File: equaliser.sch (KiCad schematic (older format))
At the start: 32 parts, among them U12 NE5532

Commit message: Board is placed and about half-routed
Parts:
- added J9: Conn_01x04_Male, Pin_Headers:Pin_Header_Straight_1x04_Pitch2.54mm, symbol Connector:Conn_01x04_Male
- C66, C67: footprint power:C_Rect_L7.0mm_W4.5mm_P5_1210x2_combo -> power:C_Rect_L19.0mm_W11.0mm_combo
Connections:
- net labels added: VFB, VO
- wire segments 83 -> 87
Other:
- note added: "Port for pluggable RC network\n(Linkwitz Transform Only)"
- moved on the sheet: U12A, U12B
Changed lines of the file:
@@
 L Amplifier_Operational:NE5532 U12
 U 2 1 61877AFD
-P 5100 3800
-F 0 "U12" H 5100 3433 50  0000 C CNN
-F 1 "NE5532" H 5100 3524 50  0000 C CNN
-F 2 "" H 5100 3800 50  0001 C CNN
-F 3 "http://www.ti.com/lit/ds/symlink/ne5532.pdf" H 5100 3800 50  0001 C CNN
-	2    5100 3800
+P 7400 3200
+F 0 "U12" H 7400 2833 50  0000 C CNN
+F 1 "NE5532" H 7400 2924 50  0000 C CNN
+F 2 "" H 7400 3200 50  0001 C CNN
+F 3 "http://www.ti.com/lit/ds/symlink/ne5532.pdf" H 7400 3200 50  0001 C CNN
+	2    7400 3200
 	1    0    0    1
 $EndComp
@@
 U 1 1 61887A13
 P 3600 3200
-F 0 "R68" V 3393 3200 50  0000 C CNN
-F 1 "R2" V 3484 3200 50  0000 C CNN
+F 0 "R68" V 3650 2950 50  0000 C CNN
+F 1 "R2" V 3300 3200 50  0000 C CNN
 F 2 "Resistors_SMD:R_0805" V 3530 3200 50  0001 C CNN
 F 3 "~" H 3600 3200 50  0001 C CNN
@@
 U 1 1 618881D6
 P 3600 3100
-F 0 "R66" V 3393 3100 50  0000 C CNN
-F 1 "R2" V 3484 3100 50  0000 C CNN
+F 0 "R66" V 3600 2850 50  0000 C CNN
+F 1 "R2" V 3300 3100 50  0000 C CNN
 F 2 "Resistors_SMD:R_0805" V 3530 3100 50  0001 C CNN
 F 3 "~" H 3600 3100 50  0001 C CNN
@@
 U 1 1 6188AB3F
 P 3600 3000
-F 0 "R64" V 3393 3000 50  0000 C CNN
-F 1 "R2" V 3484 3000 50  0000 C CNN
+F 0 "R64" V 3600 2750 50  0000 C CNN
+F 1 "R2" V 3300 3000 50  0000 C CNN
 F 2 "Resistors_SMD:R_0805" V 3530 3000 50  0001 C CNN
 F 3 "~" H 3600 3000 50  0001 C CNN
@@
 U 1 1 6188EADB
 P 4800 3200
-F 0 "R69" V 4593 3200 50  0000 C CNN
+F 0 "R69" V 4850 2950 50  0000 C CNN
 F 1 "R2" V 4684 3200 50  0000 C CNN
 F 2 "Resistors_SMD:R_0805" V 4730 3200 50  0001 C CNN
@@
 U 1 1 6188EAE1
 P 4800 3100
-F 0 "R67" V 4593 3100 50  0000 C CNN
+F 0 "R67" V 4800 2850 50  0000 C CNN
 F 1 "R2" V 4684 3100 50  0000 C CNN
 F 2 "Resistors_SMD:R_0805" V 4730 3100 50  0001 C CNN
@@
 U 1 1 6188EAE7
 P 4800 3000
-F 0 "R65" V 4593 3000 50  0000 C CNN
+F 0 "R65" V 4800 2750 50  0000 C CNN
 F 1 "R2" V 4684 3000 50  0000 C CNN
 F 2 "Resistors_SMD:R_0805" V 4730 3000 50  0001 C CNN
@@
 U 1 1 61891898
 P 3600 3900
-F 0 "R75" V 3393 3900 50  0000 C CNN
+F 0 "R75" V 3650 3650 50  0000 C CNN
 F 1 "R1" V 3484 3900 50  0000 C CNN
 F 2 "Resistors_SMD:R_0805" V 3530 3900 50  0001 C CNN
@@
 U 1 1 6189189E
 P 3600 3800
-F 0 "R73" V 3393 3800 50  0000 C CNN
+F 0 "R73" V 3600 3550 50  0000 C CNN
 F 1 "R1" V 3484 3800 50  0000 C CNN
 F 2 "Resistors_SMD:R_0805" V 3530 3800 50  0001 C CNN
@@
 U 1 1 618918A4
 P 3600 3700
-F 0 "R71" V 3393 3700 50  0000 C CNN
+F 0 "R71" V 3600 3450 50  0000 C CNN
 F 1 "R1" V 3484 3700 50  0000 C CNN
 F 2 "Resistors_SMD:R_0805" V 3530 3700 50  0001 C CNN
@@
 U 1 1 61893819
 P 4150 3900
-F 0 "R76" V 3943 3900 50  0000 C CNN
+F 0 "R76" V 4150 4150 50  0000 C CNN
 F 1 "R1" V 4034 3900 50  0000 C CNN
 F 2 "Resistors_SMD:R_0805" V 4080 3900 50  0001 C CNN
@@
 U 1 1 6189381F
 P 4150 3800
-F 0 "R74" V 3943 3800 50  0000 C CNN
+F 0 "R74" V 4150 4050 50  0000 C CNN
 F 1 "R1" V 4034 3800 50  0000 C CNN
 F 2 "Resistors_SMD:R_0805" V 4080 3800 50  0001 C CNN
@@
 U 1 1 61893825
 P 4150 3700
-F 0 "R72" V 3943 3700 50  0000 C CNN
+F 0 "R72" V 4100 3900 50  0000 C CNN
 F 1 "R1" V 4034 3700 50  0000 C CNN
 F 2 "Resistors_SMD:R_0805" V 4080 3700 50  0001 C CNN
@@
 U 1 1 618B4E04
 P 4750 2150
-F 0 "R61" V 4543 2150 50  0000 C CNN
+F 0 "R61" V 4800 1900 50  0000 C CNN
 F 1 "R3" V 4634 2150 50  0000 C CNN
 F 2 "Resistors_SMD:R_0805" V 4680 2150 50  0001 C CNN
@@
 U 1 1 618B4E0A
 P 4750 2050
-F 0 "R59" V 4543 2050 50  0000 C CNN
+F 0 "R59" V 4750 1800 50  0000 C CNN
 F 1 "R3" V 4634 2050 50  0000 C CNN
 F 2 "Resistors_SMD:R_0805" V 4680 2050 50  0001 C CNN
@@
 U 1 1 618B4E10
 P 4750 1950
-F 0 "R57" V 4543 1950 50  0000 C CNN
+F 0 "R57" V 4750 1700 50  0000 C CNN
 F 1 "R3" V 4634 1950 50  0000 C CNN
 F 2 "Resistors_SMD:R_0805" V 4680 1950 50  0001 C CNN
@@
 U 1 1 618B4E18
 P 5300 2150
-F 0 "R62" V 5093 2150 50  0000 C CNN
+F 0 "R62" V 5300 2550 50  0000 C CNN
 F 1 "R3" V 5184 2150 50  0000 C CNN
 F 2 "Resistors_SMD:R_0805" V 5230 2150 50  0001 C CNN
@@
 U 1 1 618B4E1E
 P 5300 2050
-F 0 "R60" V 5093 2050 50  0000 C CNN
+F 0 "R60" V 5300 2450 50  0000 C CNN
 F 1 "R3" V 5184 2050 50  0000 C CNN
 F 2 "Resistors_SMD:R_0805" V 5230 2050 50  0001 C CNN
@@
 U 1 1 618B4E24
 P 5300 1950
-F 0 "R58" V 5093 1950 50  0000 C CNN
+F 0 "R58" V 5250 2350 50  0000 C CNN
 F 1 "R3" V 5184 1950 50  0000 C CNN
 F 2 "Resistors_SMD:R_0805" V 5230 1950 50  0001 C CNN
@@
 F 3 "~" H 5300 2450 50  0001 C CNN
 	1    5300 2450
-	1    0    0    -1
+	-1   0    0    1
 $EndComp
 Wire Wire Line
@@
 F 0 "C66" V 5648 3300 50  0000 C CNN
 F 1 "200n" V 5739 3300 50  0000 C CNN
-F 2 "power:C_Rect_L7.0mm_W4.5mm_P5_1210x2_combo" H 5938 3150 50  0001 C CNN
+F 2 "power:C_Rect_L19.0mm_W11.0mm_combo" H 5938 3150 50  0001 C CNN
 F 3 "~" H 5900 3300 50  0001 C CNN
 	1    5900 3300
-	0    1    1    0
+	0    -1   -1   0
 $EndComp
 $Comp
 L Amplifier_Operational:NE5532 U?
 U 1 1 61F41F09
-P 7400 3200
+P 5100 3800
 AR Path="/61F41F09" Ref="U?"  Part="1"
 AR Path="/6157B871/61F41F09" Ref="U?"  Part="1"
@@
 AR Path="/615C4B54/61F41F09" Ref="U?"  Part="1"
 AR Path="/616914EE/61F41F09" Ref="U12"  Part="1"
-F 0 "U12" H 7400 2833 50  0000 C CNN
-F 1 "NE5532" H 7400 2924 50  0000 C CNN
-F 2 "Housings_DIP:DIP-8_W7.62mm_Socket" H 7400 3200 50  0001 C CNN
-F 3 "http://www.ti.com/lit/ds/symlink/ne5532.pdf" H 7400 3200 50  0001 C CNN
-	1    7400 3200
+F 0 "U12" H 5100 3433 50  0000 C CNN
+F 1 "NE5532" H 5100 3524 50  0000 C CNN
+F 2 "Housings_DIP:DIP-8_W7.62mm_Socket" H 5100 3800 50  0001 C CNN
+F 3 "http://www.ti.com/lit/ds/symlink/ne5532.pdf" H 5100 3800 50  0001 C CNN
+	1    5100 3800
 	1    0    0    1
 $EndComp
@@
 F 0 "C67" V 6198 3300 50  0000 C CNN
 F 1 "200n" V 6289 3300 50  0000 C CNN
-F 2 "power:C_Rect_L7.0mm_W4.5mm_P5_1210x2_combo" H 6488 3150 50  0001 C CNN
+F 2 "power:C_Rect_L19.0mm_W11.0mm_combo" H 6488 3150 50  0001 C CNN
 F 3 "~" H 6450 3300 50  0001 C CNN
 	1    6450 3300
 	0    1    1    0
 $EndComp
+Text Label 2600 3900 0    50   ~ 0
+IN
+Text Label 4550 3700 0    50   ~ 0
+VFB
+Text Label 5500 3800 0    50   ~ 0
+VO
+$Comp
+L Connector:Conn_01x04_Male J9
+U 1 1 61731F90
+P 4300 6600
+F 0 "J9" H 4272 6574 50  0000 R CNN
+F 1 "Conn_01x04_Male" H 4272 6483 50  0000 R CNN
+F 2 "Pin_Headers:Pin_Header_Straight_1x04_Pitch2.54mm" H 4300 6600 50  0001 C CNN
+F 3 "~" H 4300 6600 50  0001 C CNN
+	1    4300 6600
+	-1   0    0    -1
+$EndComp
+Wire Wire Line
+	4100 6500 3650 6500
+Wire Wire Line
+	4100 6600 3650 6600
+Wire Wire Line
+	4100 6700 3650 6700
+Wire Wire Line
+	4100 6800 3650 6800
+Text GLabel 3650 6600 0    50   UnSpc ~ 0
+GND
+Text Label 3800 6500 0    50   ~ 0
+IN
+Text Label 3800 6700 0    50   ~ 0
+VFB
+Text Label 3800 6800 0    50   ~ 0
+VO
+Text Notes 3650 7150 0    50   ~ 0
+Port for pluggable RC network\n(Linkwitz Transform Only)
 $EndSCHEMATC

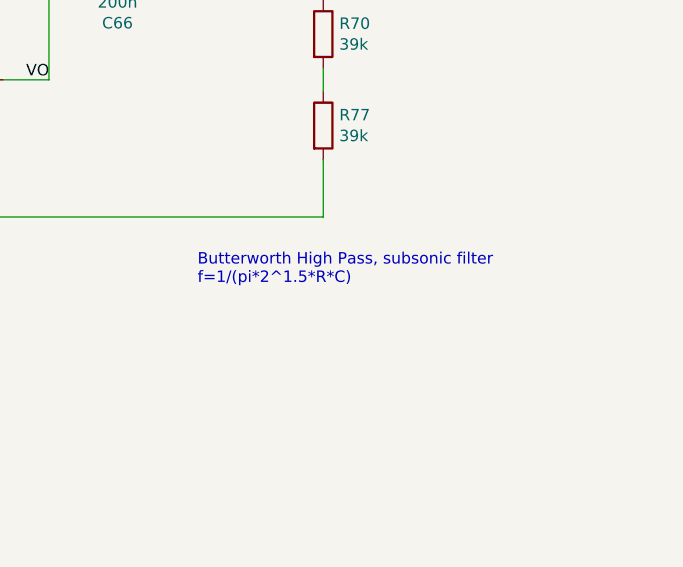
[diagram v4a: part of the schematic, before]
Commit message: Rev.B adds "hum break resistor" in input network
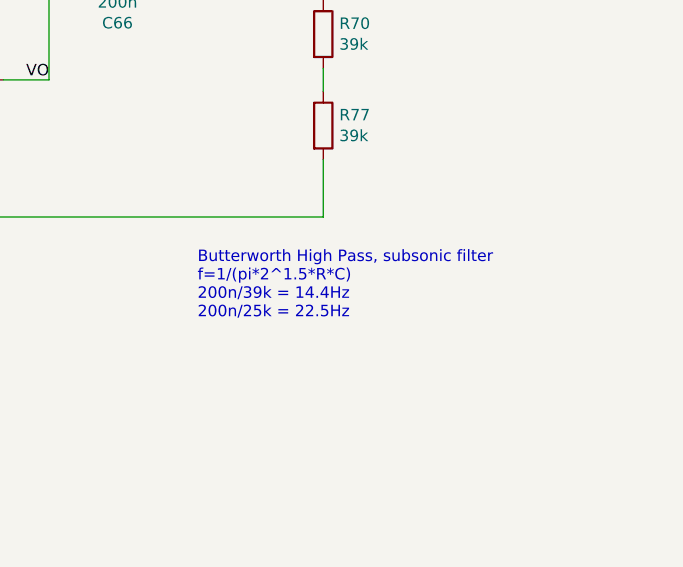
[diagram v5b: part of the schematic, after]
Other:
- note added: "Butterworth High Pass, subsonic filter\nf=1/(pi*2^1.5*R*C)\n200n/39k = 14.4Hz\n200n/25k = 22.5Hz"
- note removed: "Butterworth High Pass, subsonic filter\nf=1/(pi*2^1.5*R*C)"
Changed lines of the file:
@@
 	7800 3200 8050 3200
 Connection ~ 7800 3200
-Text Notes 6250 4700 0    50   ~ 0
-Butterworth High Pass, subsonic filter\nf=1/(pi*2^1.5*R*C)
+Text Notes 6250 4850 0    50   ~ 0
+Butterworth High Pass, subsonic filter\nf=1/(pi*2^1.5*R*C)\n200n/39k = 14.4Hz\n200n/25k = 22.5Hz
 $Comp
 L Device:C C?
